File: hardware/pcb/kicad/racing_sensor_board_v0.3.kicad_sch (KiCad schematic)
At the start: 0 parts

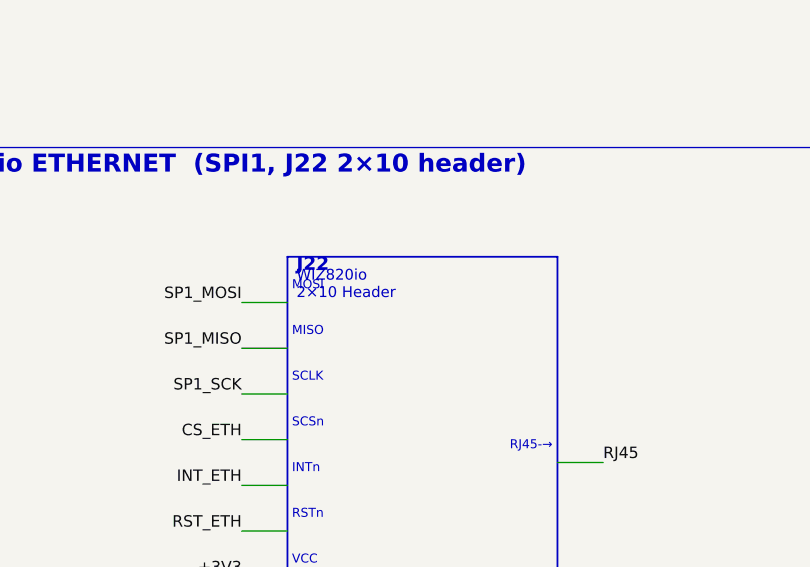
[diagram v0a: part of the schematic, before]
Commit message: Fix unterminated string in KiCad v0.3 schematic
WIZ820io label had a newline inside the quoted string which KiCad's
parser rejects. Collapsed to single line.

https://claude.ai/code/session_01NVvsy3kMr9piDWfs5WdvpG
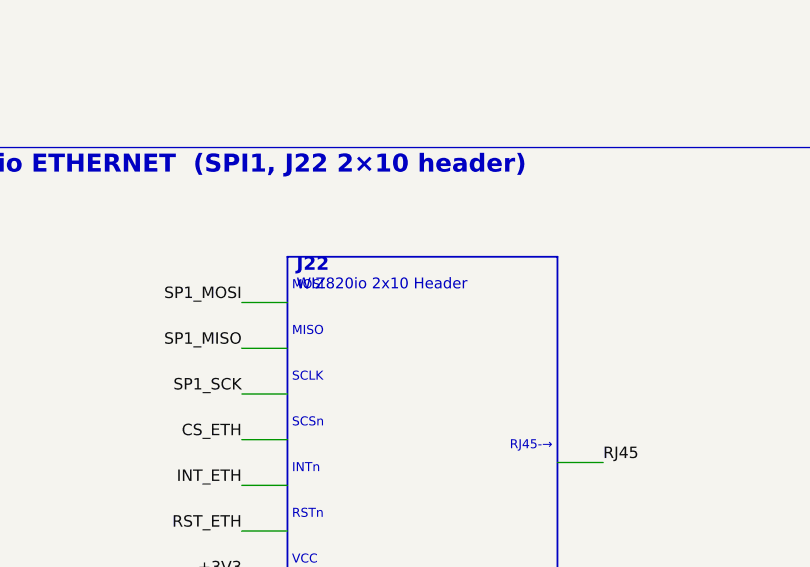
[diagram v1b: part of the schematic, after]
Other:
- note added: "WIZ820io 2x10 Header"
- note removed: "WIZ820io 2×10 Header"
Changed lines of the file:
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@@
     (effects (font (size 1.5 1.5) (bold yes))(justify left))
   )
-  (text "WIZ820io
-2×10 Header" (at 336.00 60.34 0)
+  (text "WIZ820io 2x10 Header" (at 336.00 60.34 0)
     (effects (font (size 1.2 1.2) )(justify left))
   )
